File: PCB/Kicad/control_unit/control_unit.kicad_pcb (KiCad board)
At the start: 6 copper layers, 150 x 150 mm, 82 parts, among them J1 in, J2 in, J3 in, J4 in, J5 in, J6 in, J7 in, J8 in, SW1 SW_Push, U4 7408, U57 744067

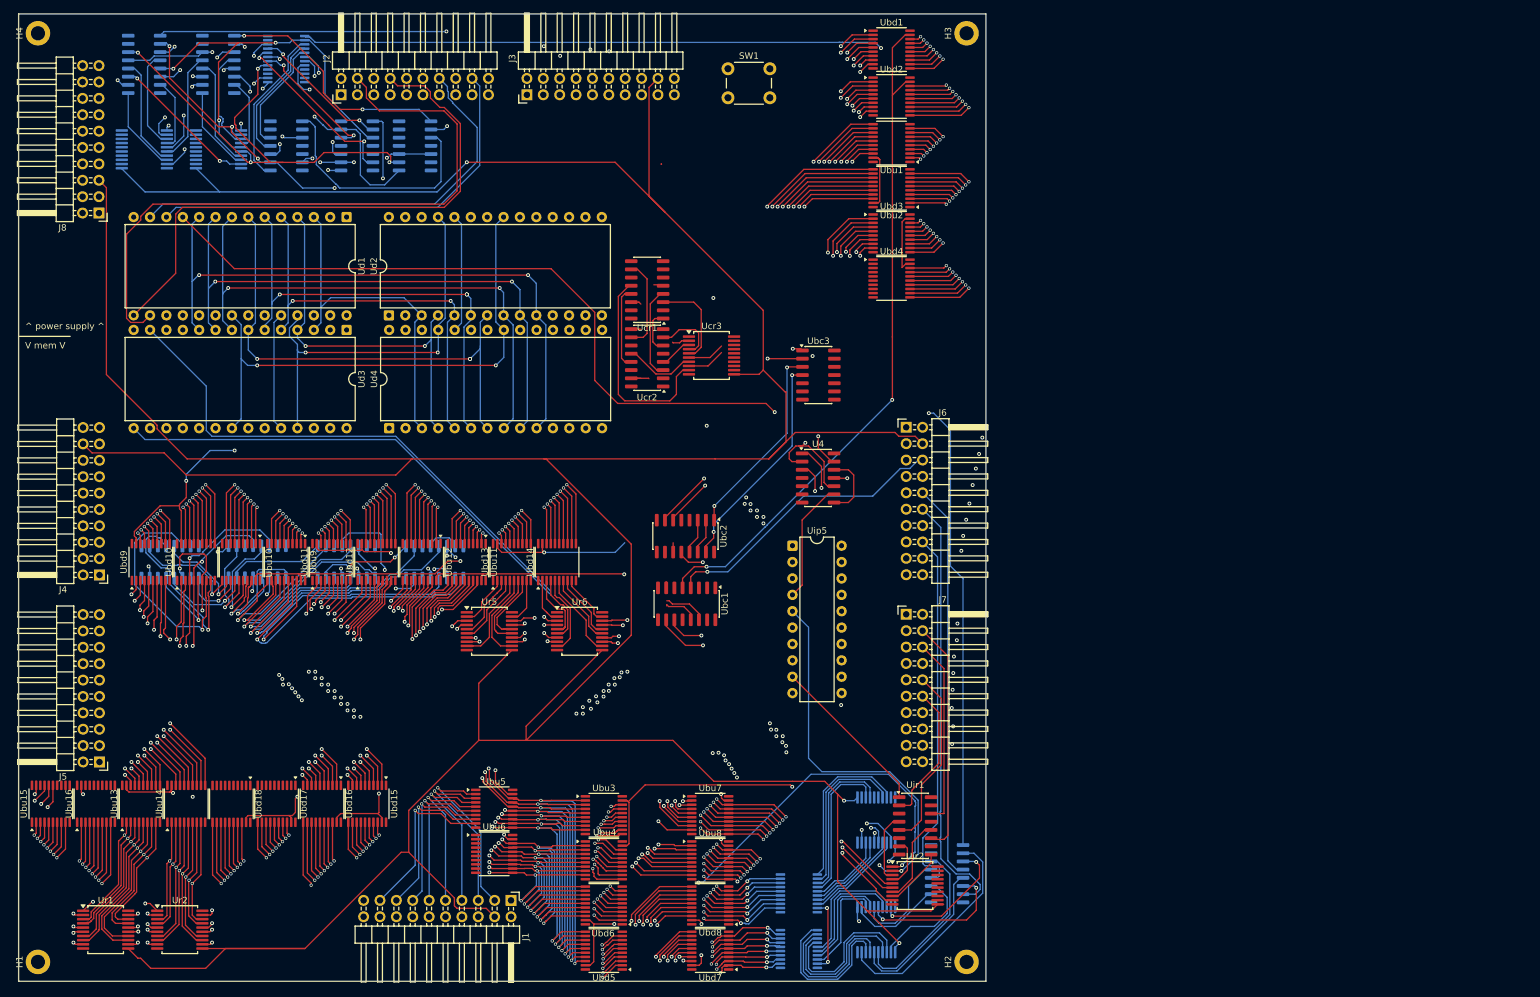
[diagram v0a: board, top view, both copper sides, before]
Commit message: control unit logic routing done
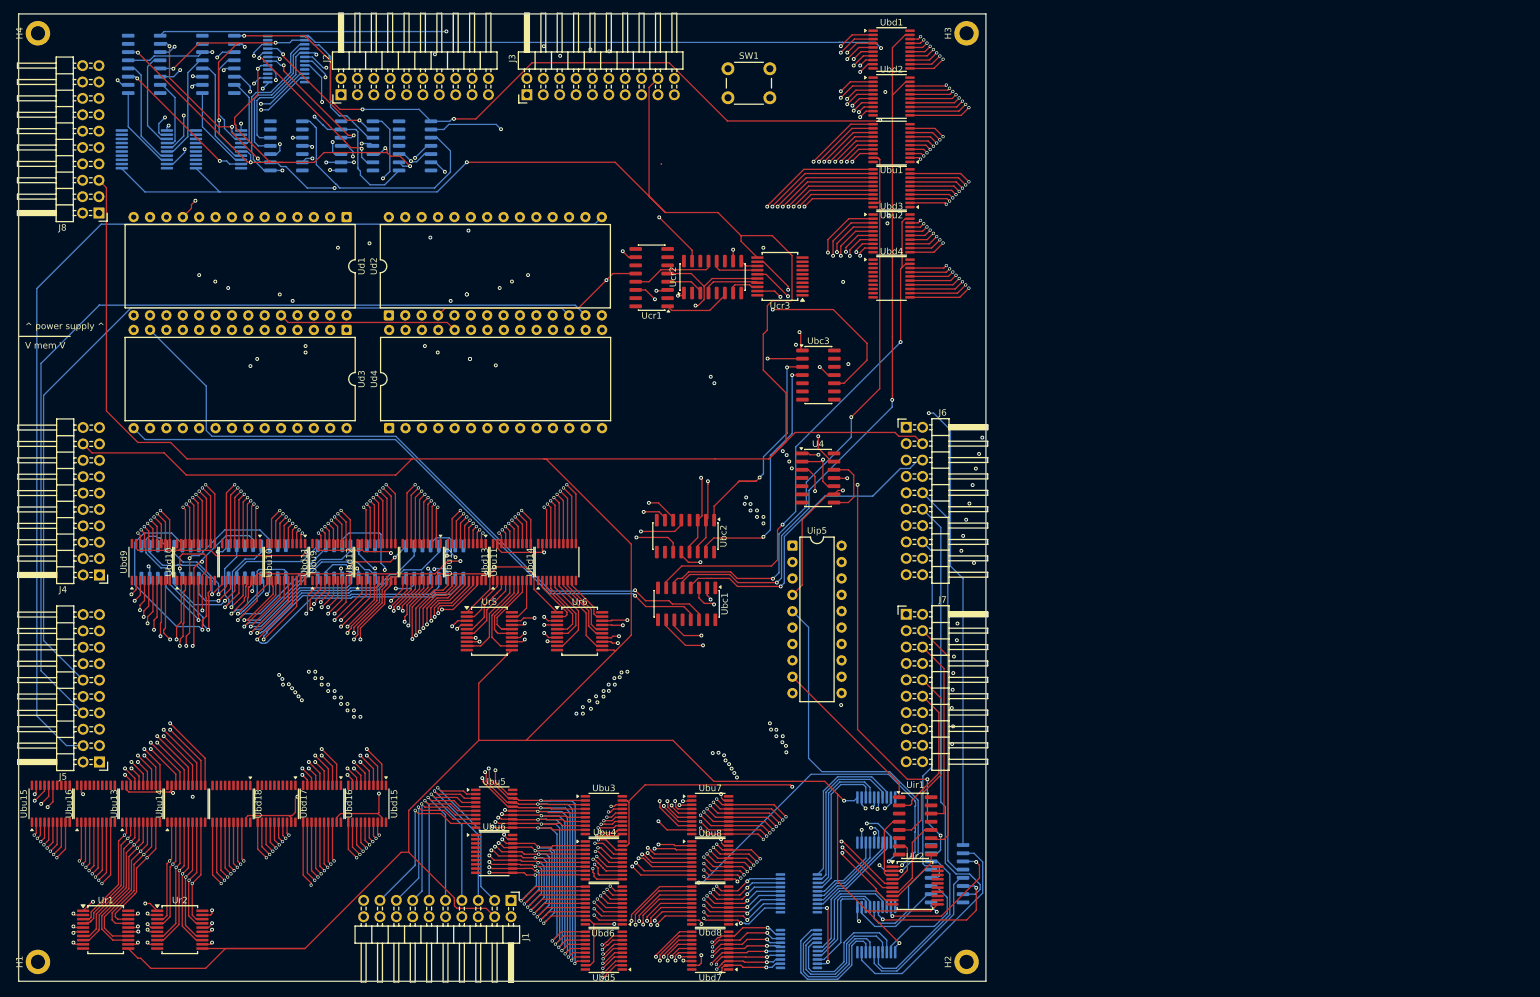
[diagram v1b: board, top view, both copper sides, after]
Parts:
- moved Ucr3 16.2 mm to (130.1, 52.7), turned to 180 degrees
- moved Ucr2 16.1 mm to (119.6, 52.8), turned to 90 degrees
- moved Ucr1 2.01 mm to (110.2, 52.9)
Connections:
- Ucr3 pad 12: unconnected-(Ucr3-Q4-Pad12) -> /ControlUnit/cycle3
- Ucr3 pad 13: VCC -> Net-(Ucr2-Zd)
- Ucr3 pad 14: VCC -> Net-(Ucr2-Zc)
- Ucr3 pad 15: unconnected-(Ucr3-Q5-Pad15) -> /ControlUnit/cycle2
- Ucr3 pad 16: unconnected-(Ucr3-Q6-Pad16) -> /ControlUnit/cycle0
- Ucr3 pad 17: VCC -> Net-(Ucr2-Za)
- Ucr3 pad 18: VCC -> Net-(Ucr2-Zb)
- Ucr3 pad 19: unconnected-(Ucr3-Q7-Pad19) -> /ControlUnit/cycle1
- Ucr3 pad 2: /ControlUnit/cycle0 -> unconnected-(Ucr3-Q0-Pad2)
- Ucr3 pad 3: Net-(Ucr2-Za) -> VCC
- Ucr3 pad 4: Net-(Ucr2-Zb) -> VCC
- Ucr3 pad 5: /ControlUnit/cycle1 -> unconnected-(Ucr3-Q1-Pad5)
- Ucr3 pad 6: /ControlUnit/cycle2 -> unconnected-(Ucr3-Q2-Pad6)
- Ucr3 pad 7: Net-(Ucr2-Zc) -> VCC
- Ucr3 pad 8: Net-(Ucr2-Zd) -> VCC
- Ucr3 pad 9: /ControlUnit/cycle3 -> unconnected-(Ucr3-Q3-Pad9)
- Ud1 pad 17: /iocmd0 -> /iocmd1
- Ud1 pad 18: /iocmd1 -> /iocmd0
- Ud2 pad 12: /memop0 -> /memop2
- Ud2 pad 15: /memop2 -> /memop0
- Ud3 pad 16: /ControlUnit/iosrc -> /ControlUnit/isstack
- Ud4 pad 11: /ControlUnit/isstack -> /ControlUnit/iosrc
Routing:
- net /ControlUnit/isstack: track 0.00 -> 178.9 mm, vias 0 -> 3
- net /ControlUnit/opcode2: track 36.8 -> 209.0 mm, vias 0 -> 2
- net /ControlUnit/opcode3: track 83.1 -> 235.7 mm, vias 2 -> 4
- net /ControlUnit/rst: track 36.3 -> 182.3 mm, vias 0 -> 2
- net /mask_save: track 49.5 -> 194.6 mm, vias 1 -> 3
- net /ControlUnit/opcode1: track 62.6 -> 206.0 mm, vias 2 -> 4
- net /mask_restore: track 87.2 -> 225.8 mm, vias 3 -> 5
- net /ControlUnit/regsrc1: track 0.00 -> 127.8 mm, vias 0 -> 2
- net /ControlUnit/isret: track 18.8 -> 145.2 mm, vias 0 -> 2
- net /ControlUnit/regsrc0: track 0.00 -> 122.4 mm, vias 0 -> 2
- net /ControlUnit/opcode0: track 78.7 -> 200.9 mm, vias 1 -> 3
- net /memop0: track 57.5 -> 167.5 mm
- net /memop1: track 51.0 -> 145.7 mm
- net /ControlUnit/memsrc2: track 30.8 -> 125.2 mm
- net /ControlUnit/memsrc0: track 5.48 -> 99.1 mm, vias 0 -> 1
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
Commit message: początek łączenia decapów
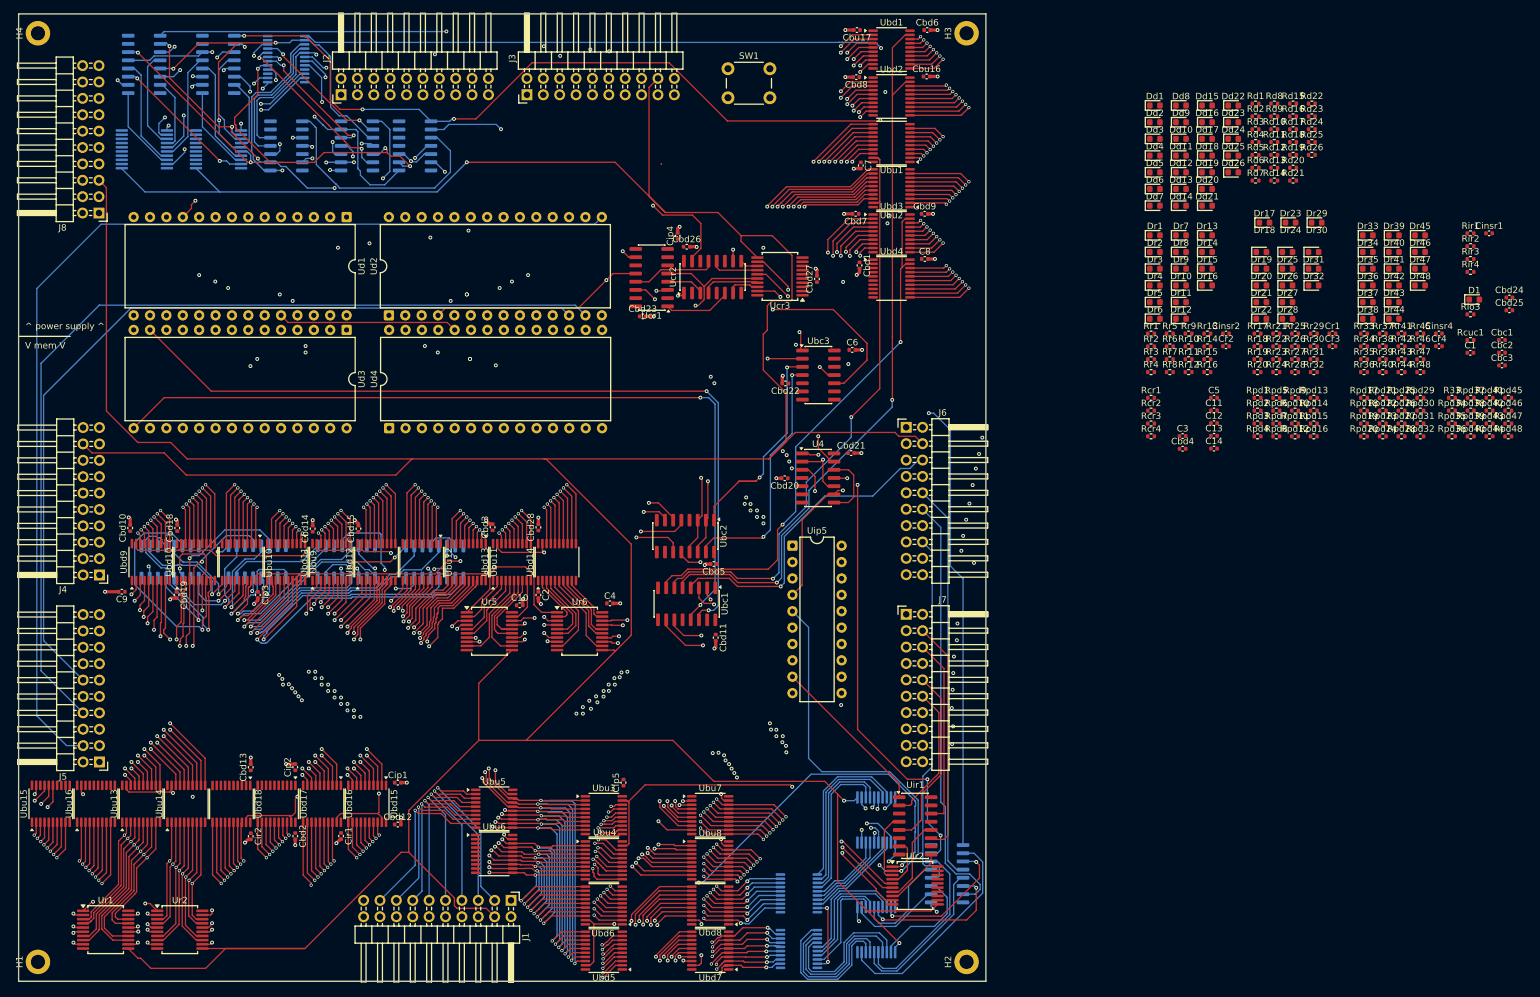
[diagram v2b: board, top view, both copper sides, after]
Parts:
- added C1: 100nF, Capacitor_SMD:C_0402_1005Metric, F.Cu at (237.1, 64.5)
- added C10: 100nF, Capacitor_SMD:C_0402_1005Metric, F.Cu at (89.7, 103.7)
- added C11: 100nF, Capacitor_SMD:C_0402_1005Metric, F.Cu at (197.4, 73.5)
- added C12: 100nF, Capacitor_SMD:C_0402_1005Metric, F.Cu at (197.4, 75.5)
- added C13: 100nF, Capacitor_SMD:C_0402_1005Metric, F.Cu at (197.4, 77.4)
- added C14: 100nF, Capacitor_SMD:C_0402_1005Metric, F.Cu at (197.4, 79.4)
- added C2: 100nF, Capacitor_SMD:C_0402_1005Metric, F.Cu at (92.6, 102.1)
- added C3: 100nF, Capacitor_SMD:C_0402_1005Metric, F.Cu at (192.5, 77.5)
- added C4: 100nF, Capacitor_SMD:C_0402_1005Metric, F.Cu at (103.7, 103.4)
- added C5: 100nF, Capacitor_SMD:C_0402_1005Metric, F.Cu at (197.4, 71.5)
- added C6: 100nF, Capacitor_SMD:C_0402_1005Metric, F.Cu at (141.3, 64.1)
- added C7: 100nF, Capacitor_SMD:C_0402_1005Metric, F.Cu at (142.6, 35.5)
- added C8: 100nF, Capacitor_SMD:C_0402_1005Metric, F.Cu at (152.5, 50.0)
- added C9: 100nF, Capacitor_SMD:C_0402_1005Metric, F.Cu at (28.0, 101.6)
- added Cbc1: 100nF, Capacitor_SMD:C_0402_1005Metric, F.Cu at (242.0, 62.6)
- added Cbc2: 100nF, Capacitor_SMD:C_0402_1005Metric, F.Cu at (242.0, 64.5)
- added Cbc3: 100nF, Capacitor_SMD:C_0402_1005Metric, F.Cu at (242.0, 66.5)
- added Cbd1: 100nF, Capacitor_SMD:C_0402_1005Metric, F.Cu at (142.4, 51.0)
- added Cbd10: 100nF, Capacitor_SMD:C_0402_1005Metric, F.Cu at (29.3, 91.7)
- added Cbd11: 100nF, Capacitor_SMD:C_0402_1005Metric, F.Cu at (120.1, 108.7)
- added Cbd12: 100nF, Capacitor_SMD:C_0402_1005Metric, F.Cu at (70.8, 137.7)
- added Cbd13: 100nF, Capacitor_SMD:C_0402_1005Metric, F.Cu at (48.0, 128.8)
- added Cbd14: 100nF, Capacitor_SMD:C_0402_1005Metric, F.Cu at (57.6, 91.8)
- added Cbd15: 100nF, Capacitor_SMD:C_0402_1005Metric, F.Cu at (64.7, 91.8)
- added Cbd18: 100nF, Capacitor_SMD:C_0402_1005Metric, F.Cu at (36.6, 91.7)
- added Cbd19: 100nF, Capacitor_SMD:C_0402_1005Metric, F.Cu at (36.5, 102.1)
- added Cbd2: 100nF, Capacitor_SMD:C_0402_1005Metric, F.Cu at (54.9, 139.5)
- added Cbd20: 100nF, Capacitor_SMD:C_0402_1005Metric, F.Cu at (130.8, 84.0)
- added Cbd21: 100nF, Capacitor_SMD:C_0402_1005Metric, F.Cu at (141.1, 80.1)
- added Cbd22: 100nF, Capacitor_SMD:C_0402_1005Metric, F.Cu at (130.9, 69.3)
- added Cbd23: 100nF, Capacitor_SMD:C_0402_1005Metric, F.Cu at (108.8, 58.9)
- added Cbd24: 100nF, Capacitor_SMD:C_0402_1005Metric, F.Cu at (243.2, 56.0)
- added Cbd25: 100nF, Capacitor_SMD:C_0402_1005Metric, F.Cu at (243.2, 58.0)
- added Cbd26: 100nF, Capacitor_SMD:C_0402_1005Metric, F.Cu at (115.6, 48.1)
- added Cbd27: 100nF, Capacitor_SMD:C_0402_1005Metric, F.Cu at (135.8, 53.1)
- added Cbd28: 100nF, Capacitor_SMD:C_0402_1005Metric, F.Cu at (92.6, 91.6)
- added Cbd3: 100nF, Capacitor_SMD:C_0402_1005Metric, F.Cu at (85.5, 91.6)
- added Cbd4: 100nF, Capacitor_SMD:C_0402_1005Metric, F.Cu at (192.5, 79.4)
- added Cbd5: 100nF, Capacitor_SMD:C_0402_1005Metric, F.Cu at (119.8, 97.3)
- added Cbd6: 100nF, Capacitor_SMD:C_0402_1005Metric, F.Cu at (152.9, 14.5)
- added Cbd7: 100nF, Capacitor_SMD:C_0402_1005Metric, F.Cu at (141.8, 43.0)
- added Cbd8: 100nF, Capacitor_SMD:C_0402_1005Metric, F.Cu at (141.9, 21.8)
- added Cbd9: 100nF, Capacitor_SMD:C_0402_1005Metric, F.Cu at (152.5, 43.0)
- added Cbu16: 100nF, Capacitor_SMD:C_0402_1005Metric, F.Cu at (152.8, 21.7)
- added Cbu17: 100nF, Capacitor_SMD:C_0402_1005Metric, F.Cu at (142.0, 14.5)
- added Cinsr1: 100nF, Capacitor_SMD:C_0402_1005Metric, F.Cu at (240.0, 46.0)
- added Cinsr2: 100nF, Capacitor_SMD:C_0402_1005Metric, F.Cu at (199.2, 61.6)
- added Cinsr4: 100nF, Capacitor_SMD:C_0402_1005Metric, F.Cu at (232.2, 61.6)
- added Cip1: 100nF, Capacitor_SMD:C_0402_1005Metric, F.Cu at (70.8, 131.2)
- added Cip2: 100nF, Capacitor_SMD:C_0402_1005Metric, F.Cu at (54.9, 128.8)
- added Cip3: 100nF, Capacitor_SMD:C_0402_1005Metric, F.Cu at (49.1, 102.1)
- added Cip4: 100nF, Capacitor_SMD:C_0402_1005Metric, F.Cu at (114.2, 46.4)
- added Cip5: 100nF, Capacitor_SMD:C_0402_1005Metric, F.Cu at (105.8, 131.2)
- added Cir1: 100nF, Capacitor_SMD:C_0402_1005Metric, F.Cu at (62.0, 139.5)
- added Cir2: 100nF, Capacitor_SMD:C_0402_1005Metric, F.Cu at (48.0, 139.5)
- added Cr1: 100nF, Capacitor_SMD:C_0402_1005Metric, F.Cu at (215.7, 61.6)
- added Cr2: 100nF, Capacitor_SMD:C_0402_1005Metric, F.Cu at (199.2, 63.5)
- added Cr3: 100nF, Capacitor_SMD:C_0402_1005Metric, F.Cu at (215.7, 63.5)
- added Cr4: 100nF, Capacitor_SMD:C_0402_1005Metric, F.Cu at (232.2, 63.5)
- added D1: green, LED_SMD:LED_0603_1608Metric, F.Cu at (237.7, 56.3)
- added Dd1: yellow, LED_SMD:LED_0603_1608Metric, F.Cu at (188.2, 26.2)
- added Dd10: yellow, LED_SMD:LED_0603_1608Metric, F.Cu at (192.2, 31.4)
- added Dd11: yellow, LED_SMD:LED_0603_1608Metric, F.Cu at (192.2, 34.0)
- added Dd12: yellow, LED_SMD:LED_0603_1608Metric, F.Cu at (192.2, 36.6)
- added Dd13: yellow, LED_SMD:LED_0603_1608Metric, F.Cu at (192.2, 39.1)
- added Dd14: yellow, LED_SMD:LED_0603_1608Metric, F.Cu at (192.2, 41.7)
- added Dd15: yellow, LED_SMD:LED_0603_1608Metric, F.Cu at (196.3, 26.2)
- added Dd16: yellow, LED_SMD:LED_0603_1608Metric, F.Cu at (196.3, 28.8)
- added Dd17: yellow, LED_SMD:LED_0603_1608Metric, F.Cu at (196.3, 31.4)
- added Dd18: yellow, LED_SMD:LED_0603_1608Metric, F.Cu at (196.3, 34.0)
- added Dd19: yellow, LED_SMD:LED_0603_1608Metric, F.Cu at (196.3, 36.6)
- added Dd2: yellow, LED_SMD:LED_0603_1608Metric, F.Cu at (188.2, 28.8)
- added Dd20: yellow, LED_SMD:LED_0603_1608Metric, F.Cu at (196.3, 39.1)
- added Dd21: yellow, LED_SMD:LED_0603_1608Metric, F.Cu at (196.3, 41.7)
- added Dd22: yellow, LED_SMD:LED_0603_1608Metric, F.Cu at (200.3, 26.2)
- added Dd23: yellow, LED_SMD:LED_0603_1608Metric, F.Cu at (200.3, 28.8)
- added Dd24: yellow, LED_SMD:LED_0603_1608Metric, F.Cu at (200.3, 31.4)
- added Dd25: yellow, LED_SMD:LED_0603_1608Metric, F.Cu at (200.3, 34.0)
- added Dd26: yellow, LED_SMD:LED_0603_1608Metric, F.Cu at (200.3, 36.6)
- added Dd3: yellow, LED_SMD:LED_0603_1608Metric, F.Cu at (188.2, 31.4)
- added Dd4: yellow, LED_SMD:LED_0603_1608Metric, F.Cu at (188.2, 34.0)
- added Dd5: yellow, LED_SMD:LED_0603_1608Metric, F.Cu at (188.2, 36.6)
- added Dd6: yellow, LED_SMD:LED_0603_1608Metric, F.Cu at (188.2, 39.1)
- added Dd7: yellow, LED_SMD:LED_0603_1608Metric, F.Cu at (188.2, 41.7)
- added Dd8: yellow, LED_SMD:LED_0603_1608Metric, F.Cu at (192.2, 26.2)
- added Dd9: yellow, LED_SMD:LED_0603_1608Metric, F.Cu at (192.2, 28.8)
- added Dr1: red, LED_SMD:LED_0603_1608Metric, F.Cu at (188.2, 46.3)
- added Dr10: red, LED_SMD:LED_0603_1608Metric, F.Cu at (192.2, 54.1)
- added Dr11: red, LED_SMD:LED_0603_1608Metric, F.Cu at (192.2, 56.7)
- added Dr12: red, LED_SMD:LED_0603_1608Metric, F.Cu at (192.2, 59.3)
- added Dr13: red, LED_SMD:LED_0603_1608Metric, F.Cu at (196.3, 46.3)
- added Dr14: red, LED_SMD:LED_0603_1608Metric, F.Cu at (196.3, 48.9)
- added Dr15: red, LED_SMD:LED_0603_1608Metric, F.Cu at (196.3, 51.5)
- added Dr16: red, LED_SMD:LED_0603_1608Metric, F.Cu at (196.3, 54.1)
- added Dr17: red, LED_SMD:LED_0603_1608Metric, F.Cu at (205.2, 44.4)
- added Dr18: red, LED_SMD:LED_0603_1608Metric, F.Cu at (204.7, 48.9)
- added Dr19: red, LED_SMD:LED_0603_1608Metric, F.Cu at (204.7, 51.5)
- added Dr2: red, LED_SMD:LED_0603_1608Metric, F.Cu at (188.2, 48.9)
- added Dr20: red, LED_SMD:LED_0603_1608Metric, F.Cu at (204.7, 54.1)
- added Dr21: red, LED_SMD:LED_0603_1608Metric, F.Cu at (204.7, 56.7)
- added Dr22: red, LED_SMD:LED_0603_1608Metric, F.Cu at (204.7, 59.3)
- added Dr23: red, LED_SMD:LED_0603_1608Metric, F.Cu at (209.2, 44.4)
- added Dr24: red, LED_SMD:LED_0603_1608Metric, F.Cu at (208.8, 48.9)
- added Dr25: red, LED_SMD:LED_0603_1608Metric, F.Cu at (208.8, 51.5)
- added Dr26: red, LED_SMD:LED_0603_1608Metric, F.Cu at (208.8, 54.1)
- added Dr27: red, LED_SMD:LED_0603_1608Metric, F.Cu at (208.8, 56.7)
- added Dr28: red, LED_SMD:LED_0603_1608Metric, F.Cu at (208.8, 59.3)
- added Dr29: red, LED_SMD:LED_0603_1608Metric, F.Cu at (213.3, 44.4)
- added Dr3: red, LED_SMD:LED_0603_1608Metric, F.Cu at (188.2, 51.5)
- added Dr30: red, LED_SMD:LED_0603_1608Metric, F.Cu at (212.8, 48.9)
- added Dr31: red, LED_SMD:LED_0603_1608Metric, F.Cu at (212.8, 51.5)
- added Dr32: red, LED_SMD:LED_0603_1608Metric, F.Cu at (212.8, 54.1)
- added Dr33: red, LED_SMD:LED_0603_1608Metric, F.Cu at (221.2, 46.3)
- added Dr34: red, LED_SMD:LED_0603_1608Metric, F.Cu at (221.2, 48.9)
- added Dr35: red, LED_SMD:LED_0603_1608Metric, F.Cu at (221.2, 51.5)
- added Dr36: red, LED_SMD:LED_0603_1608Metric, F.Cu at (221.2, 54.1)
- added Dr37: red, LED_SMD:LED_0603_1608Metric, F.Cu at (221.2, 56.7)
- added Dr38: red, LED_SMD:LED_0603_1608Metric, F.Cu at (221.2, 59.3)
- added Dr39: red, LED_SMD:LED_0603_1608Metric, F.Cu at (225.3, 46.3)
- added Dr4: red, LED_SMD:LED_0603_1608Metric, F.Cu at (188.2, 54.1)
- added Dr40: red, LED_SMD:LED_0603_1608Metric, F.Cu at (225.3, 48.9)
- added Dr41: red, LED_SMD:LED_0603_1608Metric, F.Cu at (225.3, 51.5)
- added Dr42: red, LED_SMD:LED_0603_1608Metric, F.Cu at (225.3, 54.1)
- added Dr43: red, LED_SMD:LED_0603_1608Metric, F.Cu at (225.3, 56.7)
- added Dr44: red, LED_SMD:LED_0603_1608Metric, F.Cu at (225.3, 59.3)
- added Dr45: red, LED_SMD:LED_0603_1608Metric, F.Cu at (229.3, 46.3)
- added Dr46: red, LED_SMD:LED_0603_1608Metric, F.Cu at (229.3, 48.9)
- added Dr47: red, LED_SMD:LED_0603_1608Metric, F.Cu at (229.3, 51.5)
- added Dr48: red, LED_SMD:LED_0603_1608Metric, F.Cu at (229.3, 54.1)
- added Dr5: red, LED_SMD:LED_0603_1608Metric, F.Cu at (188.2, 56.7)
- added Dr6: red, LED_SMD:LED_0603_1608Metric, F.Cu at (188.2, 59.3)
- added Dr7: red, LED_SMD:LED_0603_1608Metric, F.Cu at (192.2, 46.3)
- added Dr8: red, LED_SMD:LED_0603_1608Metric, F.Cu at (192.2, 48.9)
- added Dr9: red, LED_SMD:LED_0603_1608Metric, F.Cu at (192.2, 51.5)
- added R33: 10k, Resistor_SMD:R_0402_1005Metric, F.Cu at (234.3, 71.5)
- added Rcr1: 10k, Resistor_SMD:R_0402_1005Metric, F.Cu at (187.6, 71.5)
- added Rcr2: 10k, Resistor_SMD:R_0402_1005Metric, F.Cu at (187.6, 73.5)
- added Rcr3: 10k, Resistor_SMD:R_0402_1005Metric, F.Cu at (187.6, 75.5)
- added Rcr4: 10k, Resistor_SMD:R_0402_1005Metric, F.Cu at (187.6, 77.5)
- added Rcuc1: 10k, Resistor_SMD:R_0402_1005Metric, F.Cu at (237.1, 62.6)
- added Rd1: 680, Resistor_SMD:R_0402_1005Metric, F.Cu at (203.8, 25.9)
- added Rd10: 680, Resistor_SMD:R_0402_1005Metric, F.Cu at (206.7, 29.9)
- added Rd11: 680, Resistor_SMD:R_0402_1005Metric, F.Cu at (206.7, 31.9)
- added Rd12: 680, Resistor_SMD:R_0402_1005Metric, F.Cu at (206.7, 33.9)
- added Rd13: 680, Resistor_SMD:R_0402_1005Metric, F.Cu at (206.7, 35.9)
- added Rd14: 680, Resistor_SMD:R_0402_1005Metric, F.Cu at (206.7, 37.8)
- added Rd15: 680, Resistor_SMD:R_0402_1005Metric, F.Cu at (209.6, 25.9)
- added Rd16: 680, Resistor_SMD:R_0402_1005Metric, F.Cu at (209.6, 27.9)
- added Rd17: 680, Resistor_SMD:R_0402_1005Metric, F.Cu at (209.6, 29.9)
- added Rd18: 680, Resistor_SMD:R_0402_1005Metric, F.Cu at (209.6, 31.9)
- added Rd19: 680, Resistor_SMD:R_0402_1005Metric, F.Cu at (209.6, 33.9)
- added Rd2: 680, Resistor_SMD:R_0402_1005Metric, F.Cu at (203.8, 27.9)
- added Rd20: 680, Resistor_SMD:R_0402_1005Metric, F.Cu at (209.6, 35.9)
- added Rd21: 680, Resistor_SMD:R_0402_1005Metric, F.Cu at (209.6, 37.8)
- added Rd22: 680, Resistor_SMD:R_0402_1005Metric, F.Cu at (212.5, 25.9)
- added Rd23: 680, Resistor_SMD:R_0402_1005Metric, F.Cu at (212.5, 27.9)
- added Rd24: 680, Resistor_SMD:R_0402_1005Metric, F.Cu at (212.5, 29.9)
- added Rd25: 680, Resistor_SMD:R_0402_1005Metric, F.Cu at (212.5, 31.9)
- added Rd26: 680, Resistor_SMD:R_0402_1005Metric, F.Cu at (212.5, 33.9)
- added Rd3: 680, Resistor_SMD:R_0402_1005Metric, F.Cu at (203.8, 29.9)
- added Rd4: 680, Resistor_SMD:R_0402_1005Metric, F.Cu at (203.8, 31.9)
- added Rd5: 680, Resistor_SMD:R_0402_1005Metric, F.Cu at (203.8, 33.9)
- added Rd6: 680, Resistor_SMD:R_0402_1005Metric, F.Cu at (203.8, 35.9)
- added Rd7: 680, Resistor_SMD:R_0402_1005Metric, F.Cu at (203.8, 37.8)
- added Rd8: 680, Resistor_SMD:R_0402_1005Metric, F.Cu at (206.7, 25.9)
- added Rd9: 680, Resistor_SMD:R_0402_1005Metric, F.Cu at (206.7, 27.9)
- added Rio3: 680, Resistor_SMD:R_0402_1005Metric, F.Cu at (237.1, 58.6)
- added Rir1: 10k, Resistor_SMD:R_0402_1005Metric, F.Cu at (237.1, 46.0)
- added Rir2: 10k, Resistor_SMD:R_0402_1005Metric, F.Cu at (237.1, 48.0)
- added Rir3: 10k, Resistor_SMD:R_0402_1005Metric, F.Cu at (237.1, 50.0)
- added Rir4: 10k, Resistor_SMD:R_0402_1005Metric, F.Cu at (237.1, 52.0)
- added Rpd1: 10k, Resistor_SMD:R_0402_1005Metric, F.Cu at (204.1, 71.5)
- added Rpd10: 10k, Resistor_SMD:R_0402_1005Metric, F.Cu at (209.9, 73.5)
- added Rpd11: 10k, Resistor_SMD:R_0402_1005Metric, F.Cu at (209.9, 75.5)
- added Rpd12: 10k, Resistor_SMD:R_0402_1005Metric, F.Cu at (209.9, 77.5)
- added Rpd13: 10k, Resistor_SMD:R_0402_1005Metric, F.Cu at (212.8, 71.5)
- added Rpd14: 10k, Resistor_SMD:R_0402_1005Metric, F.Cu at (212.8, 73.5)
- added Rpd15: 10k, Resistor_SMD:R_0402_1005Metric, F.Cu at (212.8, 75.5)
- added Rpd16: 10k, Resistor_SMD:R_0402_1005Metric, F.Cu at (212.8, 77.5)
- added Rpd17: 10k, Resistor_SMD:R_0402_1005Metric, F.Cu at (220.6, 71.5)
- added Rpd18: 10k, Resistor_SMD:R_0402_1005Metric, F.Cu at (220.6, 73.5)
- added Rpd19: 10k, Resistor_SMD:R_0402_1005Metric, F.Cu at (220.6, 75.5)
- added Rpd2: 10k, Resistor_SMD:R_0402_1005Metric, F.Cu at (204.1, 73.5)
- added Rpd20: 10k, Resistor_SMD:R_0402_1005Metric, F.Cu at (220.6, 77.5)
- added Rpd21: 10k, Resistor_SMD:R_0402_1005Metric, F.Cu at (223.5, 71.5)
- added Rpd22: 10k, Resistor_SMD:R_0402_1005Metric, F.Cu at (223.5, 73.5)
- added Rpd23: 10k, Resistor_SMD:R_0402_1005Metric, F.Cu at (223.5, 75.5)
- added Rpd24: 10k, Resistor_SMD:R_0402_1005Metric, F.Cu at (223.5, 77.5)
- added Rpd25: 10k, Resistor_SMD:R_0402_1005Metric, F.Cu at (226.4, 71.5)
- added Rpd26: 10k, Resistor_SMD:R_0402_1005Metric, F.Cu at (226.4, 73.5)
- added Rpd27: 10k, Resistor_SMD:R_0402_1005Metric, F.Cu at (226.4, 75.5)
- added Rpd28: 10k, Resistor_SMD:R_0402_1005Metric, F.Cu at (226.4, 77.5)
- added Rpd29: 10k, Resistor_SMD:R_0402_1005Metric, F.Cu at (229.4, 71.5)
- added Rpd3: 10k, Resistor_SMD:R_0402_1005Metric, F.Cu at (204.1, 75.5)
- added Rpd30: 10k, Resistor_SMD:R_0402_1005Metric, F.Cu at (229.4, 73.5)
- added Rpd31: 10k, Resistor_SMD:R_0402_1005Metric, F.Cu at (229.4, 75.5)
- added Rpd32: 10k, Resistor_SMD:R_0402_1005Metric, F.Cu at (229.4, 77.5)
- added Rpd34: 10k, Resistor_SMD:R_0402_1005Metric, F.Cu at (234.3, 73.5)
- added Rpd35: 10k, Resistor_SMD:R_0402_1005Metric, F.Cu at (234.3, 75.5)
- added Rpd36: 10k, Resistor_SMD:R_0402_1005Metric, F.Cu at (234.3, 77.5)
- added Rpd37: 10k, Resistor_SMD:R_0402_1005Metric, F.Cu at (237.2, 71.5)
- added Rpd38: 10k, Resistor_SMD:R_0402_1005Metric, F.Cu at (237.2, 73.5)
- added Rpd39: 10k, Resistor_SMD:R_0402_1005Metric, F.Cu at (237.2, 75.5)
- added Rpd4: 10k, Resistor_SMD:R_0402_1005Metric, F.Cu at (204.1, 77.5)
- added Rpd40: 10k, Resistor_SMD:R_0402_1005Metric, F.Cu at (237.2, 77.5)
- added Rpd41: 10k, Resistor_SMD:R_0402_1005Metric, F.Cu at (240.1, 71.5)
- added Rpd42: 10k, Resistor_SMD:R_0402_1005Metric, F.Cu at (240.1, 73.5)
- added Rpd43: 10k, Resistor_SMD:R_0402_1005Metric, F.Cu at (240.1, 75.5)
- added Rpd44: 10k, Resistor_SMD:R_0402_1005Metric, F.Cu at (240.1, 77.5)
- added Rpd45: 10k, Resistor_SMD:R_0402_1005Metric, F.Cu at (243.0, 71.5)
- added Rpd46: 10k, Resistor_SMD:R_0402_1005Metric, F.Cu at (243.0, 73.5)
- added Rpd47: 10k, Resistor_SMD:R_0402_1005Metric, F.Cu at (243.0, 75.5)
- added Rpd48: 10k, Resistor_SMD:R_0402_1005Metric, F.Cu at (243.0, 77.5)
- added Rpd5: 10k, Resistor_SMD:R_0402_1005Metric, F.Cu at (207.0, 71.5)
- added Rpd6: 10k, Resistor_SMD:R_0402_1005Metric, F.Cu at (207.0, 73.5)
- added Rpd7: 10k, Resistor_SMD:R_0402_1005Metric, F.Cu at (207.0, 75.5)
- added Rpd8: 10k, Resistor_SMD:R_0402_1005Metric, F.Cu at (207.0, 77.5)
- added Rpd9: 10k, Resistor_SMD:R_0402_1005Metric, F.Cu at (209.9, 71.5)
- added Rr1: 680, Resistor_SMD:R_0402_1005Metric, F.Cu at (187.6, 61.6)
- added Rr10: 680, Resistor_SMD:R_0402_1005Metric, F.Cu at (193.4, 63.6)
- added Rr11: 680, Resistor_SMD:R_0402_1005Metric, F.Cu at (193.4, 65.5)
- added Rr12: 680, Resistor_SMD:R_0402_1005Metric, F.Cu at (193.4, 67.5)
- added Rr13: 680, Resistor_SMD:R_0402_1005Metric, F.Cu at (196.3, 61.6)
- added Rr14: 680, Resistor_SMD:R_0402_1005Metric, F.Cu at (196.3, 63.6)
- added Rr15: 680, Resistor_SMD:R_0402_1005Metric, F.Cu at (196.3, 65.5)
- added Rr16: 680, Resistor_SMD:R_0402_1005Metric, F.Cu at (196.3, 67.5)
- added Rr17: 680, Resistor_SMD:R_0402_1005Metric, F.Cu at (204.1, 61.6)
- added Rr18: 680, Resistor_SMD:R_0402_1005Metric, F.Cu at (204.1, 63.6)
- added Rr19: 680, Resistor_SMD:R_0402_1005Metric, F.Cu at (204.1, 65.5)
- added Rr2: 680, Resistor_SMD:R_0402_1005Metric, F.Cu at (187.6, 63.6)
- added Rr20: 680, Resistor_SMD:R_0402_1005Metric, F.Cu at (204.1, 67.5)
- added Rr21: 680, Resistor_SMD:R_0402_1005Metric, F.Cu at (207.0, 61.6)
- added Rr22: 680, Resistor_SMD:R_0402_1005Metric, F.Cu at (207.0, 63.6)
- added Rr23: 680, Resistor_SMD:R_0402_1005Metric, F.Cu at (207.0, 65.5)
- added Rr24: 680, Resistor_SMD:R_0402_1005Metric, F.Cu at (207.0, 67.5)
- added Rr25: 680, Resistor_SMD:R_0402_1005Metric, F.Cu at (209.9, 61.6)
- added Rr26: 680, Resistor_SMD:R_0402_1005Metric, F.Cu at (209.9, 63.6)
- added Rr27: 680, Resistor_SMD:R_0402_1005Metric, F.Cu at (209.9, 65.5)
- added Rr28: 680, Resistor_SMD:R_0402_1005Metric, F.Cu at (209.9, 67.5)
- added Rr29: 680, Resistor_SMD:R_0402_1005Metric, F.Cu at (212.8, 61.6)
- added Rr3: 680, Resistor_SMD:R_0402_1005Metric, F.Cu at (187.6, 65.5)
- added Rr30: 680, Resistor_SMD:R_0402_1005Metric, F.Cu at (212.8, 63.6)
- added Rr31: 680, Resistor_SMD:R_0402_1005Metric, F.Cu at (212.8, 65.5)
- added Rr32: 680, Resistor_SMD:R_0402_1005Metric, F.Cu at (212.8, 67.5)
- added Rr33: 680, Resistor_SMD:R_0402_1005Metric, F.Cu at (220.6, 61.6)
- added Rr34: 680, Resistor_SMD:R_0402_1005Metric, F.Cu at (220.6, 63.6)
- added Rr35: 680, Resistor_SMD:R_0402_1005Metric, F.Cu at (220.6, 65.5)
- added Rr36: 680, Resistor_SMD:R_0402_1005Metric, F.Cu at (220.6, 67.5)
- added Rr37: 680, Resistor_SMD:R_0402_1005Metric, F.Cu at (223.5, 61.6)
- added Rr38: 680, Resistor_SMD:R_0402_1005Metric, F.Cu at (223.5, 63.6)
- added Rr39: 680, Resistor_SMD:R_0402_1005Metric, F.Cu at (223.5, 65.5)
- added Rr4: 680, Resistor_SMD:R_0402_1005Metric, F.Cu at (187.6, 67.5)
- added Rr40: 680, Resistor_SMD:R_0402_1005Metric, F.Cu at (223.5, 67.5)
- added Rr41: 680, Resistor_SMD:R_0402_1005Metric, F.Cu at (226.4, 61.6)
- added Rr42: 680, Resistor_SMD:R_0402_1005Metric, F.Cu at (226.4, 63.6)
- added Rr43: 680, Resistor_SMD:R_0402_1005Metric, F.Cu at (226.4, 65.5)
- added Rr44: 680, Resistor_SMD:R_0402_1005Metric, F.Cu at (226.4, 67.5)
- added Rr45: 680, Resistor_SMD:R_0402_1005Metric, F.Cu at (229.4, 61.6)
- added Rr46: 680, Resistor_SMD:R_0402_1005Metric, F.Cu at (229.4, 63.6)
- added Rr47: 680, Resistor_SMD:R_0402_1005Metric, F.Cu at (229.4, 65.5)
- added Rr48: 680, Resistor_SMD:R_0402_1005Metric, F.Cu at (229.4, 67.5)
- added Rr5: 680, Resistor_SMD:R_0402_1005Metric, F.Cu at (190.5, 61.6)
- added Rr6: 680, Resistor_SMD:R_0402_1005Metric, F.Cu at (190.5, 63.6)
- added Rr7: 680, Resistor_SMD:R_0402_1005Metric, F.Cu at (190.5, 65.5)
- added Rr8: 680, Resistor_SMD:R_0402_1005Metric, F.Cu at (190.5, 67.5)
- added Rr9: 680, Resistor_SMD:R_0402_1005Metric, F.Cu at (193.4, 61.6)
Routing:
- net GND: track 0.00 -> 43.0 mm, vias 0 -> 38
- net /ControlUnit/alusrc1: track 99.3 -> 127.5 mm, vias 1 -> 2
- net /ControlUnit/alusrc0: track 108.4 -> 128.8 mm, vias 1 -> 2
- net /ControlUnit/rst: track 182.3 -> 187.2 mm
- net /membus4: track 364.2 -> 367.6 mm
- net /membus6: track 373.5 -> 376.8 mm
- net /membus5: track 369.5 -> 372.8 mm
- net /membus3: track 364.0 -> 366.4 mm
- net /membus7: track 378.0 -> 380.4 mm
- net /membus2: track 360.3 -> 362.6 mm
- net /ControlUnit/buscntrl/srcbus3: track 86.3 -> 88.2 mm
- net /ControlUnit/buscntrl/srcbus2: track 85.7 -> 87.5 mm
- net /ControlUnit/buscntrl/srcbus0: track 85.6 -> 87.4 mm
- net /membus1: track 360.9 -> 362.7 mm
- net /ControlUnit/buscntrl/srcbus1: track 86.2 -> 87.8 mm
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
